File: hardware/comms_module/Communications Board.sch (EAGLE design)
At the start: 74 parts, among them U1 Value, U2 STC3115, X2 USB-MICROB, Y1 32.768kHz, Y2 24MHz

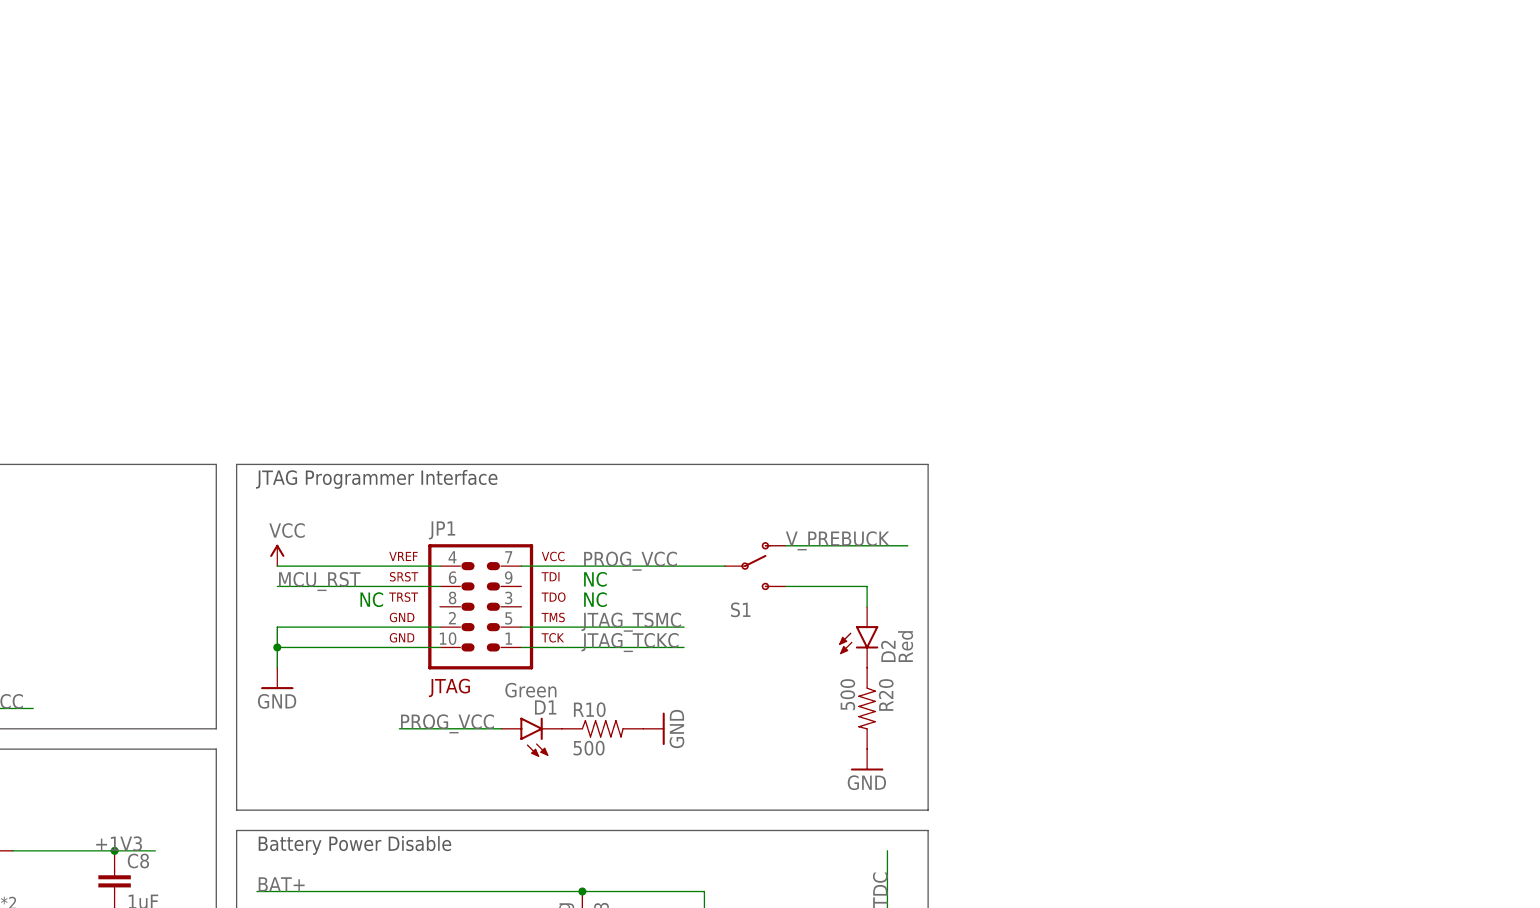
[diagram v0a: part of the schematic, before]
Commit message: Add programming attachment board.
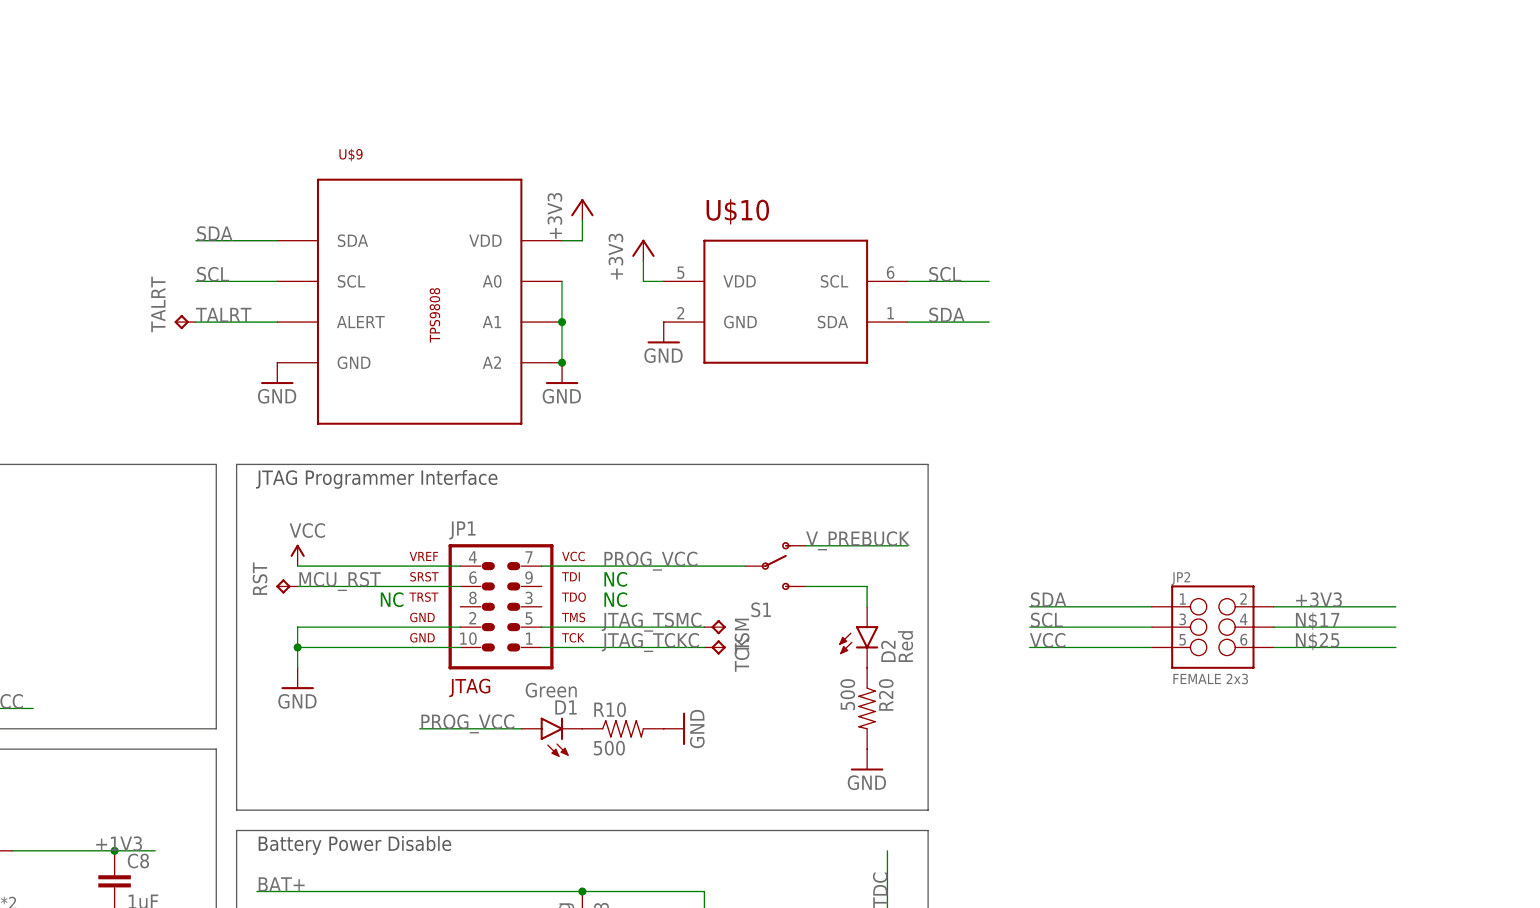
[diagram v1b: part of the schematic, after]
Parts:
- added JP2: FEMALE 2x3, SparkFun-Connectors:M03X2FEMALE
- added RST, TALRT, TCK, TSM: TPTP17R, testpad:TPTP17R
- added U$10: HDC1050, Capstone Library:HDC1050
- added U$9: MCP9808, Capstone Library:MCP9808
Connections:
- new net N$17: JP2.4
- new net N$25: JP2.6
- new net TALRT: TALRT.TP, U$9.ALERT
- net +3V3: now also JP2.2, U$10.VDD, U$9.VDD
- net GND: now also U$10.GND, U$9.A0, U$9.A1, U$9.A2, U$9.GND
- net JTAG_TCKC: now also TCK.TP
- net JTAG_TSMC: now also TSM.TP
- net MCU_RST: now also RST.TP
- net SCL: now also JP2.3, U$10.SCL, U$9.SCL
- net SDA: now also JP2.1, U$10.SDA, U$9.SDA
- net VCC: now also JP2.5
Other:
- moved on the sheet: D1, JP1, R10, S1

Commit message: Complete programming/debug attachment board.
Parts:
- added +1V3: TPTP10R, testpad:TPTP10R
- added C25, C26: 100nF, SparkFun-Passives:CAP0402-CAP
- added D3, D4, D5, D6, D7, D8: Green, SparkFun-LED:LED1206
- added R21, R22, R23, R24, R25, R26: 180, SparkFun-Passives:RESISTOR0603-RES
- added R27, R28: 10k, SparkFun-Passives:RESISTOR0603-RES
- added R29, R30: 1Meg, SparkFun-Passives:RESISTOR0402-RES
- added TS1, TS2: (no value), SparkFun-Connectors:M02PTH
- added U3: TCA9554A_PW_16, Capstone Library:TCA9554A_PW_16
- JP2: value FEMALE 2x3 -> (none); device SparkFun-Connectors:M03X2FEMALE -> SparkFun-Connectors:M03PTH
- RST, TCK, TSM: value TPTP17R -> TPTP10R; device testpad:TPTP17R -> testpad:TPTP10R
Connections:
- removed net DBG_LED: U$1.Y7
- removed net N$25: JP2.6
- new net N$11: C25.1, R27.1, TS1.1, U3.P1
- new net N$13: D4.A, U3.P5
- new net N$15: D5.A, U3.P6
- new net N$28: D8.A, U3.P2
- new net N$29: D7.A, U3.P3
- new net N$30: D3.C, R21.1
- new net N$31: D4.C, R22.1
- new net N$32: D5.C, R23.1
- new net N$33: D6.C, R24.1
- new net N$34: D7.C, R25.1
- new net N$35: D8.C, R26.1
- new net N$36: C26.1, R28.1, TS2.1, U3.P0
- new net N$7: D3.A, U3.P4
- new net V_PREBUCK_DIV2: R29.1, R30.2, U$1.Y7
- net +1V3: now also +1V3.TP
- net +3V3: now also TS1.2, TS2.2, U3.A0, U3.A1, U3.A2, U3.VCC; no longer JP2.2
- net GND: now also C25.2, C26.2, R21.2, R22.2, R23.2, R24.2, R25.2, R26.2, R27.2, R28.2, R30.1, U3.GND
- net N$17: now also D6.A, U3.P7; no longer JP2.4
- net SCL: now also JP2.2, U3.SCL; no longer JP2.3
- net SDA: now also JP2.3, U3.SDA; no longer JP2.1
- net VCC: now also JP2.1; no longer JP2.5
- net V_PREBUCK: now also R29.2
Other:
- note added: "V_PREBUCK May be >3.3V"

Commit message: Create muiltiple schematic sheets, and organize
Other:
- note added: "Debug Peripherals (Debug Attachment)"
- note added: "Inter-Board Connectors"
- note added: "MCU"
- note added: "MCU Power Management"
- note added: "Moisture Sensing Selector"
- note removed: "VCC is for MCU high-frequency domain and is seperated by a GHz noise filter from 3.3V."
